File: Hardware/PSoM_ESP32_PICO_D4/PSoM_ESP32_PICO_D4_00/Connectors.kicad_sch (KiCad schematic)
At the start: 4 parts, among them J101 DF40C-60DP-0.4V(51)

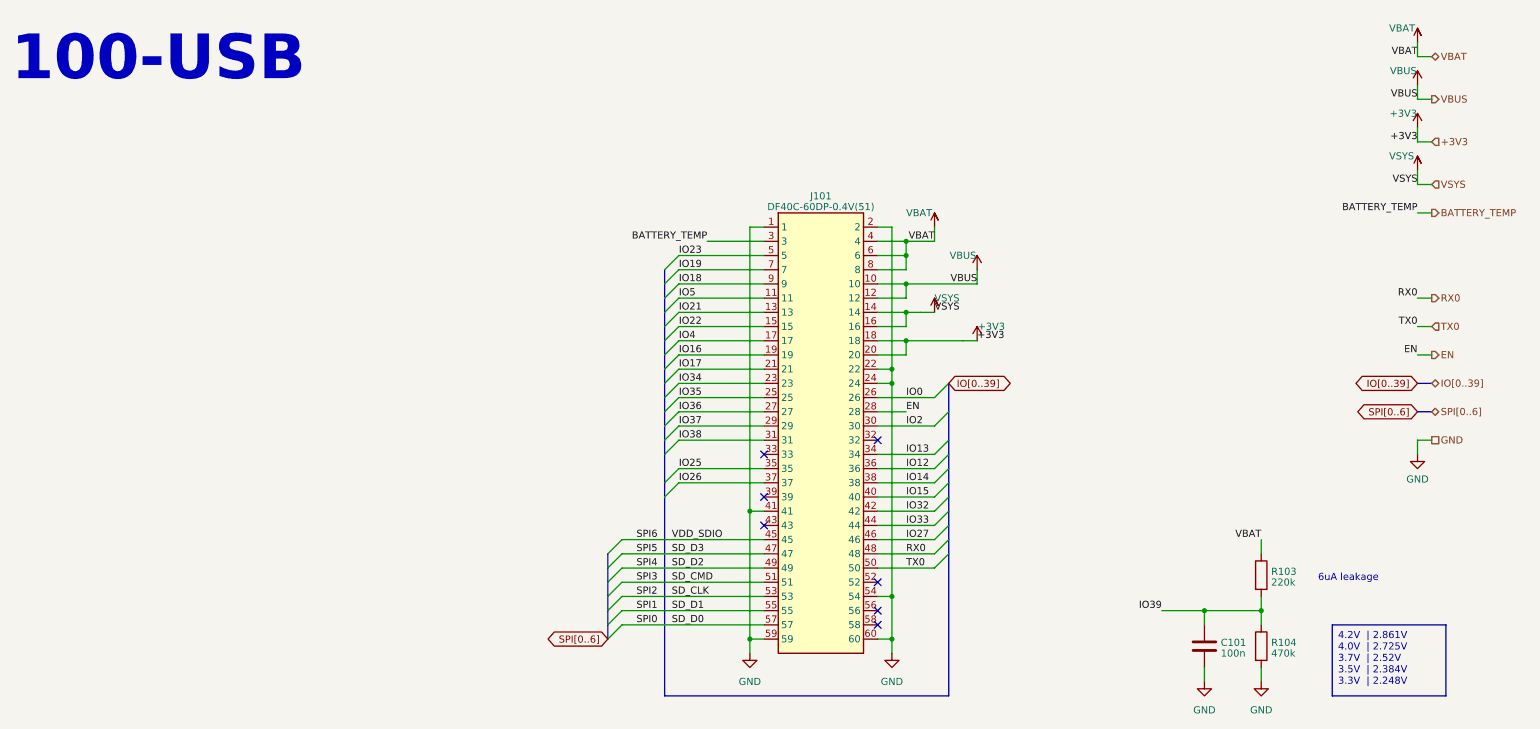
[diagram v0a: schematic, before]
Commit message: Final pinout for PSoM_ESP32_PICO_D4
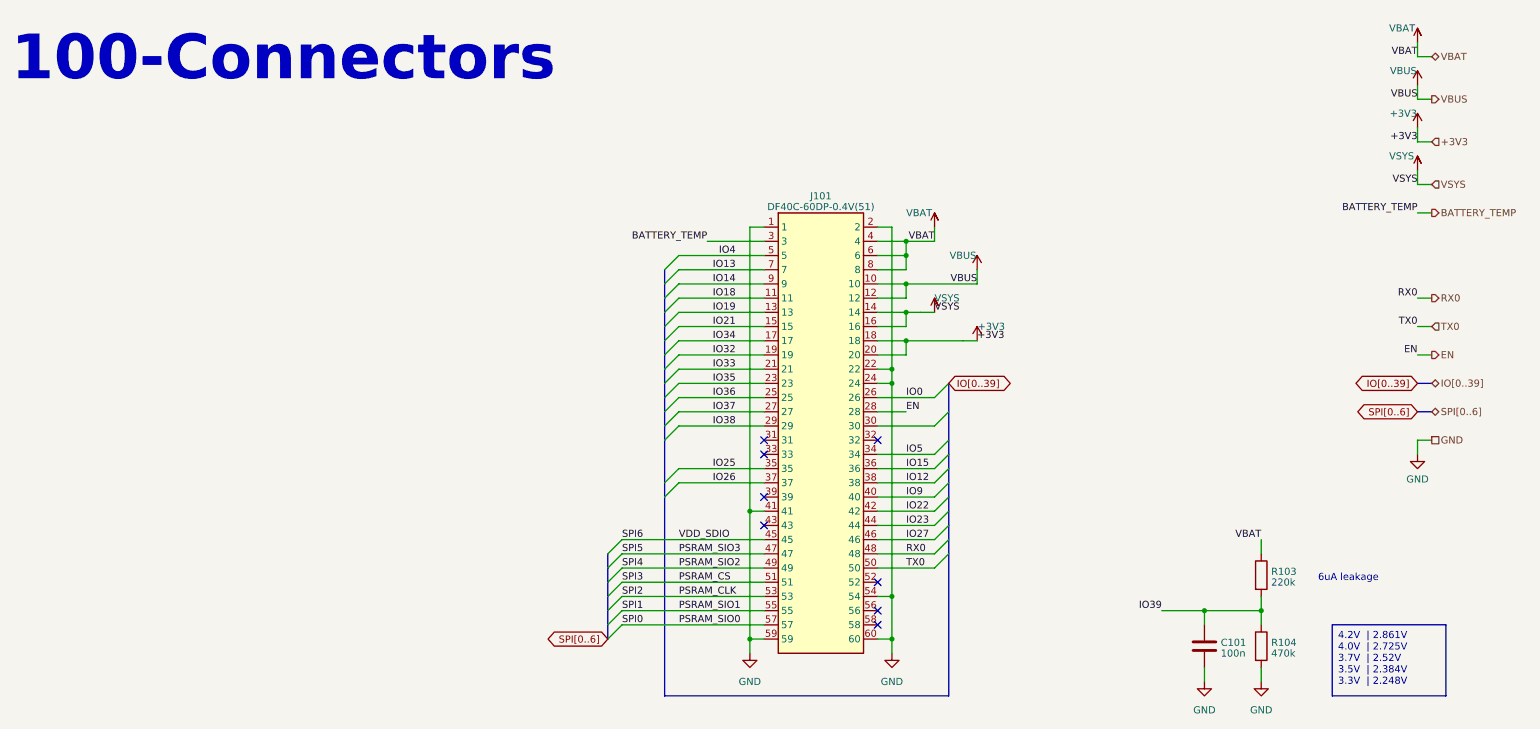
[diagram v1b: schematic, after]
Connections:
- net IO16 is gone; now on net IO32: J101.19
- net IO17 is gone; now on net IO33: J101.21
- net IO12: now also J101.38; no longer J101.36
- net IO13: now also J101.7; no longer J101.34
- net IO14: now also J101.9; no longer J101.38
- net IO15: now also J101.36; no longer J101.40
- net IO18: now also J101.11; no longer J101.9
- net IO19: now also J101.13; no longer J101.7
- net IO21: now also J101.15; no longer J101.13
- net IO22: now also J101.42; no longer J101.15
- net IO23: now also J101.44; no longer J101.5
- net IO32: no longer J101.42
- net IO33: no longer J101.44
- net IO34: now also J101.17; no longer J101.23
- net IO35: now also J101.23; no longer J101.25
- net IO36: now also J101.25; no longer J101.27
- net IO37: now also J101.27; no longer J101.29
- net IO38: now also J101.29; no longer J101.31
- net IO4: now also J101.5; no longer J101.17
- net IO5: now also J101.34; no longer J101.11
- net IO2: no longer names the net of J101.30
- net SD_CLK renamed PSRAM_CLK
- net SD_CMD renamed PSRAM_CS
- net SD_D0 renamed PSRAM_SIO0
- net SD_D1 renamed PSRAM_SIO1
- net SD_D2 renamed PSRAM_SIO2
- net SD_D3 renamed PSRAM_SIO3
- new net IO9: J101.40
- no-connect marks 7 -> 8
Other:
- note added: "100-Connectors"
- note removed: "100-USB"
